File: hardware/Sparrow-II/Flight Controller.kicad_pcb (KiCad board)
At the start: 4 copper layers, 42 x 42 mm, 114 parts

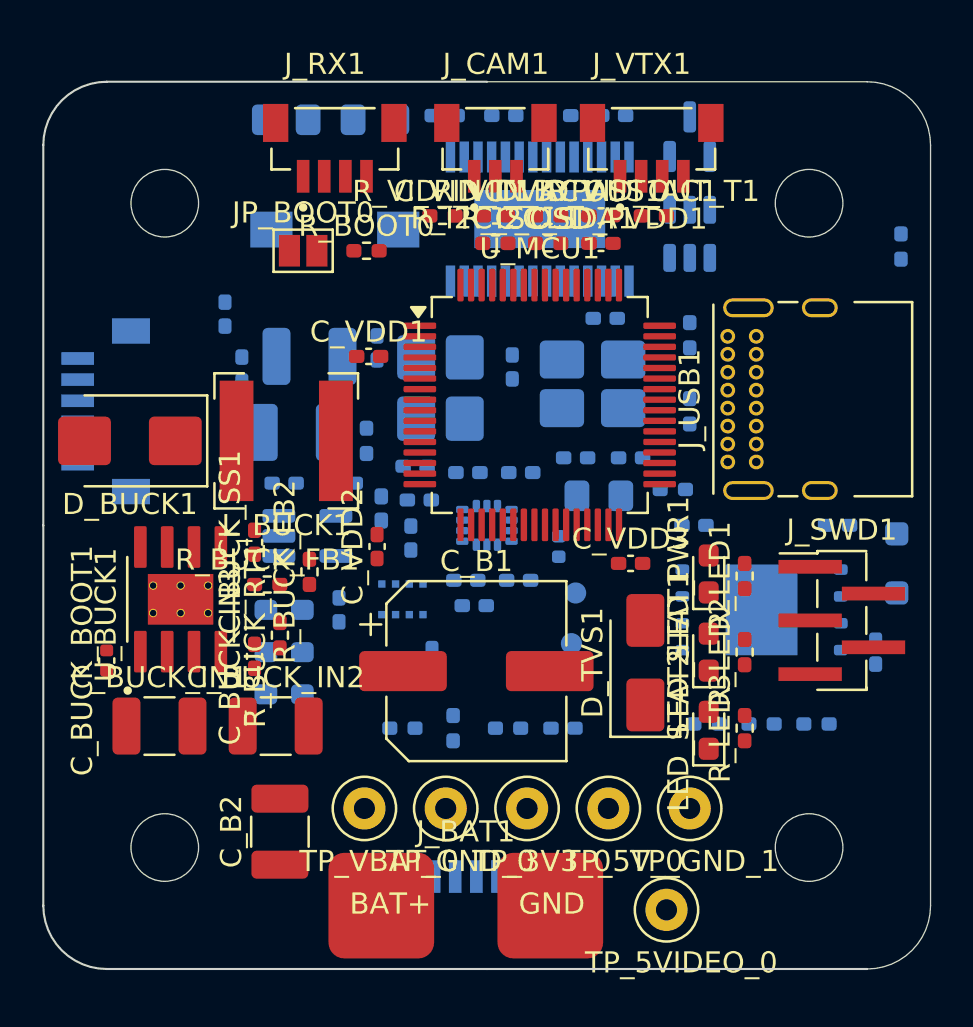
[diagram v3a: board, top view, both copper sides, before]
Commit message: hardware: BOM actualization and second layout
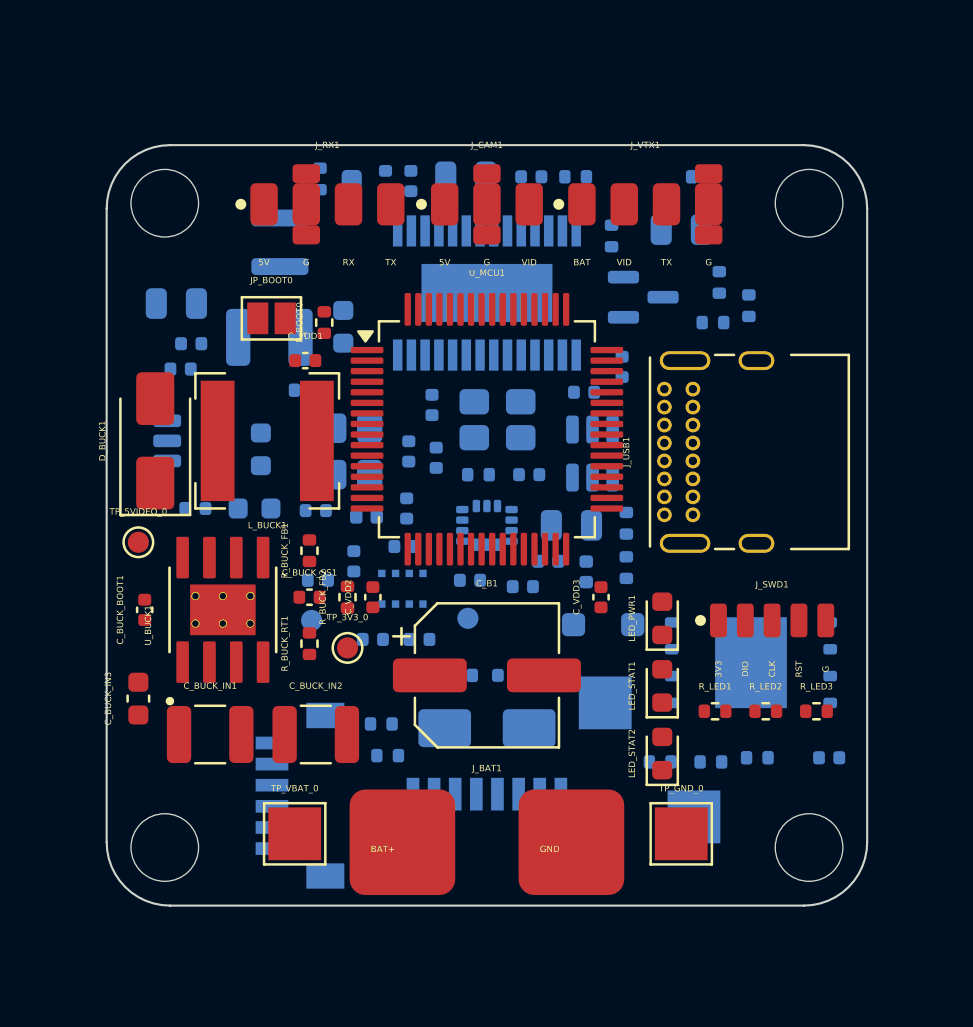
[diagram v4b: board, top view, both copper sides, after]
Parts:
- removed C_B2: 10uF, Capacitor_SMD:C_1210_3225Metric_Pad1.33x2.70mm_HandSolder
- removed C_B3: 1uF, Capacitor_SMD:C_0603_1608Metric_Pad1.08x0.95mm_HandSolder
- removed C_B4: 100nF, Capacitor_SMD:C_0402_1005Metric_Pad0.74x0.62mm_HandSolder
- removed C_BUCK_OUT2: 47uF, Capacitor_SMD:C_1210_3225Metric_Pad1.33x2.70mm_HandSolder
- removed C_USB_SH1: 10nF, Capacitor_SMD:C_0402_1005Metric_Pad0.74x0.62mm_HandSolder
- removed C_VID2: 22uF, Capacitor_SMD:C_0805_2012Metric_Pad1.18x1.45mm_HandSolder
- C_3V3_BULK1, C_5V_BULK1: footprint Capacitor_SMD:C_0603_1608Metric_Pad1.08x0.95mm_HandSolder -> Capacitor_SMD:C_0603_1608Metric
- C_B1: value 470uF -> 100uF; footprint Capacitor_SMD:CP_Elec_8x6.9 -> Capacitor_SMD:CP_Elec_6.3x7.7
- C_BARO1, C_BARO2, C_BUCK_SS1, C_CURR_F1, C_FLASH1, C_HSE1, C_HSE2, C_IMU_VDD1, C_IMU_VDD2, C_IMU_VIO1, C_IMU_VIO2, C_LDO_IN1, C_LDO_OUT1, C_NRST1, C_OSD_AVDD1, C_OSD_DVDD1, C_OSD_PVDD2, C_OSD_XTAL1, C_OSD_XTAL2, C_VBAT_ADC1, C_VDD1, C_VDD2, C_VDD3, C_VDD4, C_VDDA1, C_VDDA_HF1, C_VID3: footprint Capacitor_SMD:C_0402_1005Metric_Pad0.74x0.62mm_HandSolder -> Capacitor_SMD:C_0402_1005Metric
- C_BUCK_IN1, C_BUCK_IN2: value 2.2uF -> 4.7uF; footprint Capacitor_SMD:C_1210_3225Metric_Pad1.33x2.70mm_HandSolder -> Capacitor_SMD:C_1210_3225Metric
- C_BUCK_IN3, C_VDD_BULK1: footprint Capacitor_SMD:C_0402_1005Metric_Pad0.74x0.62mm_HandSolder -> Capacitor_SMD:C_0603_1608Metric
- C_BUCK_OUT1: footprint Capacitor_SMD:C_1210_3225Metric_Pad1.33x2.70mm_HandSolder -> Capacitor_SMD:C_1210_3225Metric
- C_OSD_PVDD1: footprint Capacitor_SMD:C_0402_1005Metric_Pad0.74x0.62mm_HandSolder -> Capacitor_SMD:C_0603_1608Metric; moved to B.Cu
- C_OSD_SAG1: footprint Capacitor_SMD:C_0402_1005Metric_Pad0.74x0.62mm_HandSolder -> Capacitor_SMD:C_0805_2012Metric
- C_VCAP1, C_VID1: footprint Capacitor_SMD:C_0805_2012Metric_Pad1.18x1.45mm_HandSolder -> Capacitor_SMD:C_0805_2012Metric
- C_VID_IN_AC1: footprint Capacitor_SMD:C_0402_1005Metric_Pad0.74x0.62mm_HandSolder -> Capacitor_SMD:C_0402_1005Metric; moved to B.Cu
- C_VID_OUT_AC1: footprint Capacitor_SMD:C_0402_1005Metric_Pad0.74x0.62mm_HandSolder -> Capacitor_SMD:C_0805_2012Metric; moved to B.Cu
- D_BUCK1: value B560C-13-F -> B260A-13-F; footprint Diode_SMD:D_SMB -> Diode_SMD:D_SMA
- D_TVS1: moved to B.Cu
- FB_VDDA1: footprint Inductor_SMD:L_0402_1005Metric_Pad0.77x0.64mm_HandSolder -> Inductor_SMD:L_0402_1005Metric
- J_CAM1: value BM03B-SRSS-TB_LF__SN_ -> CAM Pads; footprint SparrowHawk:JST_BM03B-SRSS-TB_LF__SN_ -> SparrowHawk:SolderPads_CAM_1x03
- J_RX1: value BM04B-SRSS-TB_LF__SN_ -> RX Pads; footprint SparrowHawk:JST_BM04B-SRSS-TB_LF__SN_ -> SparrowHawk:SolderPads_RX_1x04
- J_SWD1: value Conn_01x05 -> SWD Pads; footprint Connector_PinHeader_1.27mm:PinHeader_1x05_P1.27mm_Vertical_SMD_Pin1Left -> SparrowHawk:SolderPads_SWD_1x05
- J_VTX1: value BM04B-SRSS-TB_LF__SN_ -> VTX Pads; footprint SparrowHawk:JST_BM04B-SRSS-TB_LF__SN_ -> SparrowHawk:SolderPads_VTX_1x04
- LED_PWR1, LED_STAT1, LED_STAT2: footprint LED_SMD:LED_0603_1608Metric_Pad1.05x0.95mm_HandSolder -> LED_SMD:LED_0603_1608Metric
- L_VID1: footprint Inductor_SMD:L_Wuerth_WE-PD-Typ-7345 -> Inductor_SMD:L_Sunlord_SWPA3015S
- R_BOOT0, R_BUCK_FB1, R_BUCK_FB2, R_BUCK_RT1, R_CC1, R_CC2, R_CURR_F1, R_FLASH_CS1, R_FLASH_HD1, R_FLASH_WP1, R_HSE1, R_HSE2, R_LED1, R_LED2, R_LED3, R_OSD_RST1, R_VBAT_D1, R_VBAT_D2: footprint Resistor_SMD:R_0402_1005Metric_Pad0.72x0.64mm_HandSolder -> Resistor_SMD:R_0402_1005Metric
- R_I2C_SCL1, R_I2C_SDA1, R_VID_BYPASS1, R_VID_IN_T1, R_VID_OUT_T1: footprint Resistor_SMD:R_0402_1005Metric_Pad0.72x0.64mm_HandSolder -> Resistor_SMD:R_0402_1005Metric; moved to B.Cu
- R_USB_SH1: value 1M -> 0R; footprint Resistor_SMD:R_0402_1005Metric_Pad0.72x0.64mm_HandSolder -> Resistor_SMD:R_0402_1005Metric
- TP_3V3_0, TP_5VIDEO_0: value Test Point Loop -> Test Point; footprint TestPoint:TestPoint_Loop_D1.80mm_Drill1.0mm_Beaded -> TestPoint:TestPoint_Pad_D1.0mm
- TP_5V_0, TP_GND_1: value Test Point Loop -> Solder Pad; footprint TestPoint:TestPoint_Loop_D1.80mm_Drill1.0mm_Beaded -> TestPoint:TestPoint_Pad_2.5x2.5mm; moved to B.Cu
- TP_GND_0, TP_VBAT_0: value Test Point Loop -> Solder Pad; footprint TestPoint:TestPoint_Loop_D1.80mm_Drill1.0mm_Beaded -> TestPoint:TestPoint_Pad_2.5x2.5mm
- U_LDO1: footprint Package_TO_SOT_SMD:SOT-23-5_HandSoldering -> Package_TO_SOT_SMD:SOT-23-5
- Y_HSE1, Y_OSD1: footprint Crystal:Crystal_SMD_3225-4Pin_3.2x2.5mm_HandSoldering -> Crystal:Crystal_SMD_3225-4Pin_3.2x2.5mm
- moved TP_5VIDEO_0 30.5 mm to (133.5, 100.8)
- moved J_GPS1 20.4 mm to (141.6, 112.8)
- moved R_CC2 18.5 mm to (156.6, 99.9)
- moved D_USB_VBUS1 14.2 mm to (155.5, 104.7), turned to 0 degrees
- moved TP_VBAT_ADC_0 12.3 mm to (141.7, 104.5)
- moved C_OSD_PVDD1 12.0 mm to (143.6, 84.4), turned to 90 degrees
- moved C_5V_BULK1 11.7 mm to (139.3, 96.4), turned to 90 degrees
- moved TP_3V3_0 11.4 mm to (143.4, 105.8)
- moved U_ESD1 11.4 mm to (155.0, 96.6)
- moved TP_GND_0 11.2 mm to (159.2, 114.6)
- moved R_I2C_SCL1 11.0 mm to (160.7, 90.4)
- moved C_VBAT_ADC1 10.6 mm to (142.0, 102.6), turned to 0 degrees
- moved C_VID1 10.1 mm to (135.3, 89.5)
- moved R_I2C_SDA1 9.95 mm to (162.4, 89.6), turned to 90 degrees
- moved R_HSE1 9.23 mm to (149.6, 97.6)
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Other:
- board size 42 x 42 mm -> 36 x 36 mm

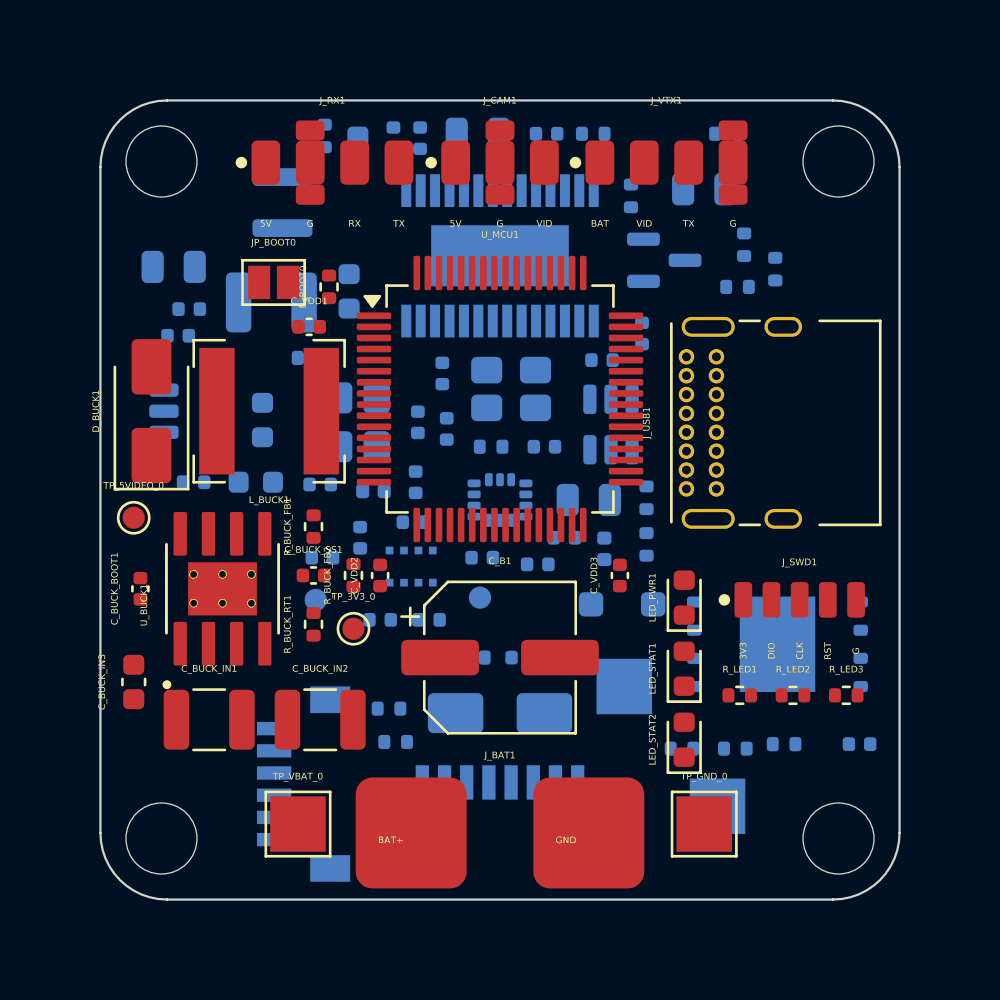
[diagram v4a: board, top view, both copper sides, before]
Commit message: hardware: Layout improvement
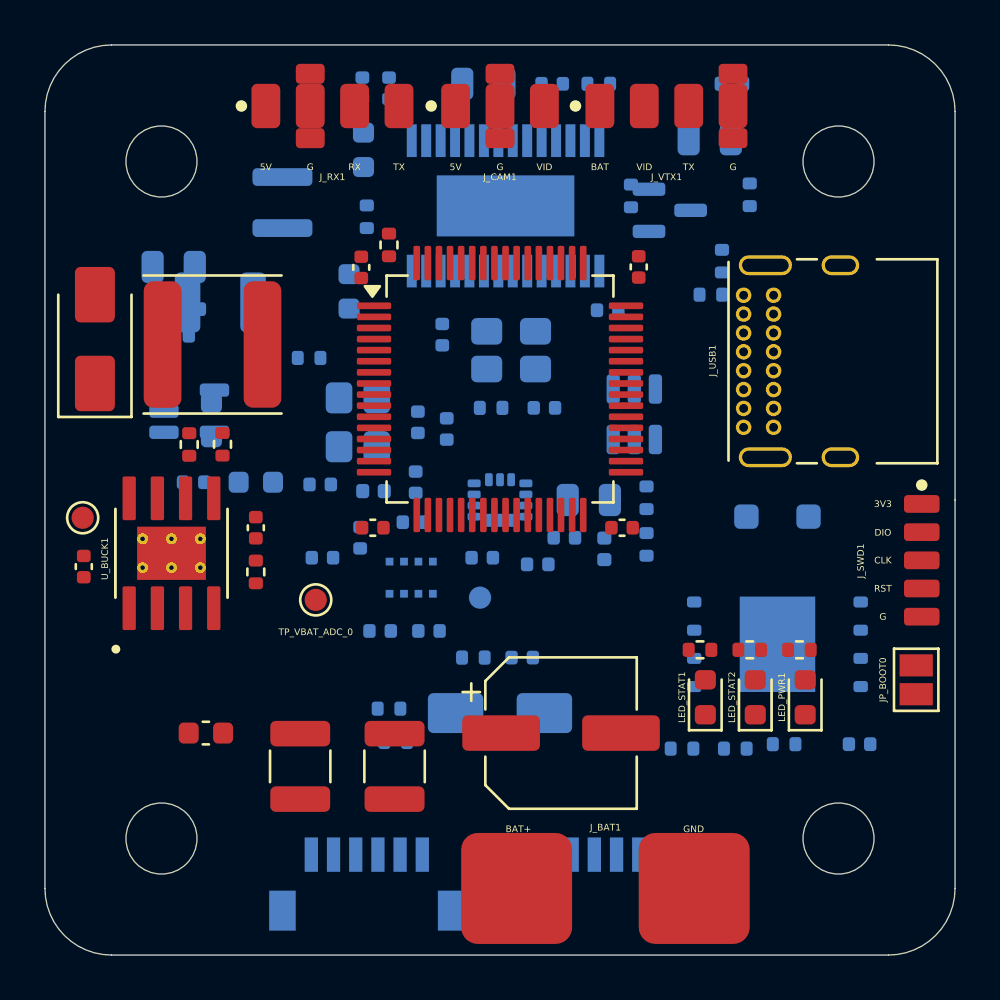
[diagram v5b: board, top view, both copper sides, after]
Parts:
- removed TP_3V3_0: Test Point, TestPoint:TestPoint_Pad_D1.0mm
- removed TP_5V_0, TP_GND_0, TP_GND_1, TP_VBAT_0: Solder Pad, TestPoint:TestPoint_Pad_2.5x2.5mm
- C_VDD4, TP_VBAT_ADC_0: moved to F.Cu
- L_BUCK1: footprint Inductor_SMD:L_Bourns-SRN6028 -> SparrowHawk:L_Sunlord_SWPA6028S
- moved JP_BOOT0 34.0 mm to (168.8, 108.1), turned to 90 degrees
- moved R_BUCK_FB2 8.35 mm to (137.5, 97.5), turned to -90 degrees
- moved D_USB_VBUS1 8.04 mm to (162.5, 100.8)
- moved LED_PWR1 7.06 mm to (163.8, 108.9)
- moved R_BUCK_FB1 6.71 mm to (136.0, 97.5)
- moved J_ESC1 6.60 mm to (155.8, 117.8)
- moved J_SWD1 5.78 mm to (169.0, 102.7), turned to -90 degrees
- moved J_GPS1 5.50 mm to (144.0, 117.8), turned to 0 degrees
- moved J_BAT1 5.37 mm to (154.8, 117.5)
- moved R_LED3 4.81 mm to (161.2, 106.8)
- moved R_LED2 4.66 mm to (159.0, 106.8)
- moved C_BUCK_IN1 4.61 mm to (141.0, 112.0), turned to -90 degrees
- moved C_B1 4.37 mm to (152.8, 110.5)
- moved D_BUCK1 4.13 mm to (131.8, 92.8)
- moved R_OSD_RST1 4.11 mm to (144.0, 87.2), turned to -90 degrees
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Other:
- board size 36 x 36 mm -> 41 x 41 mm

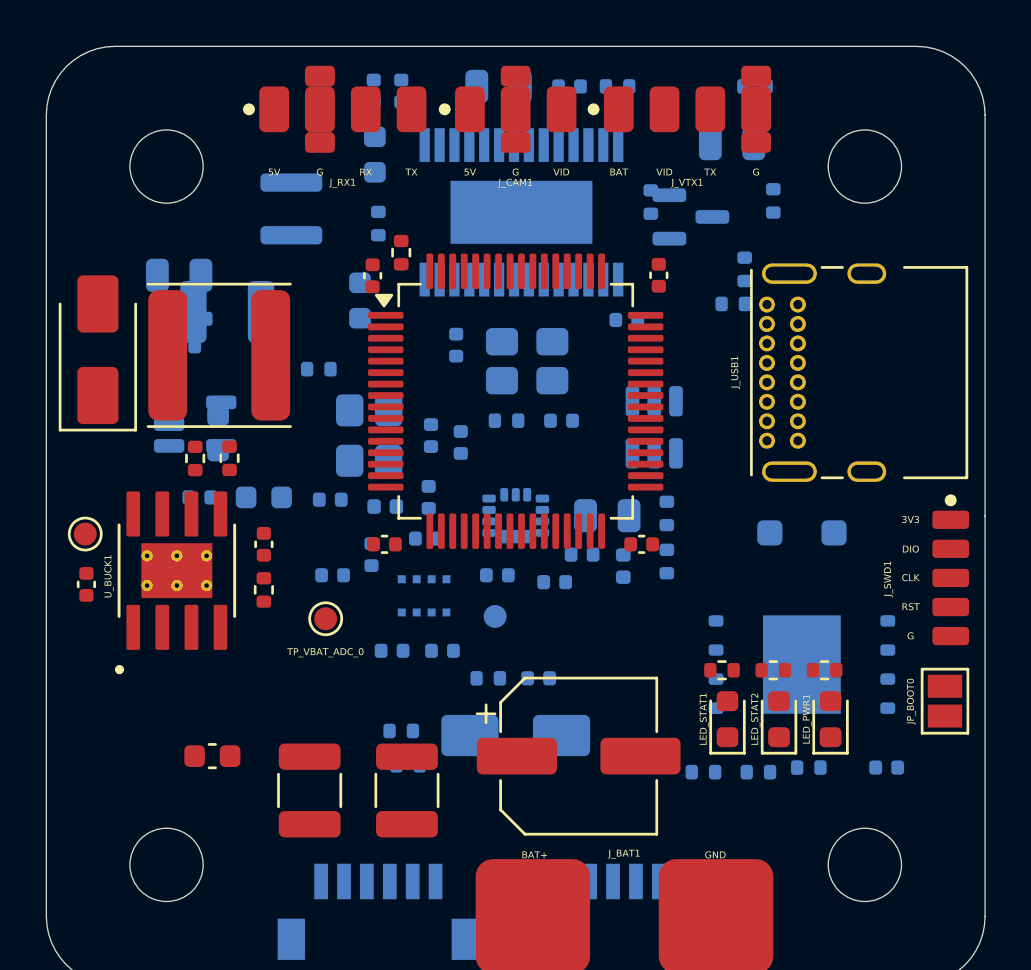
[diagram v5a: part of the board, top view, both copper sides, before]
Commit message: hardware: Fixes in layout
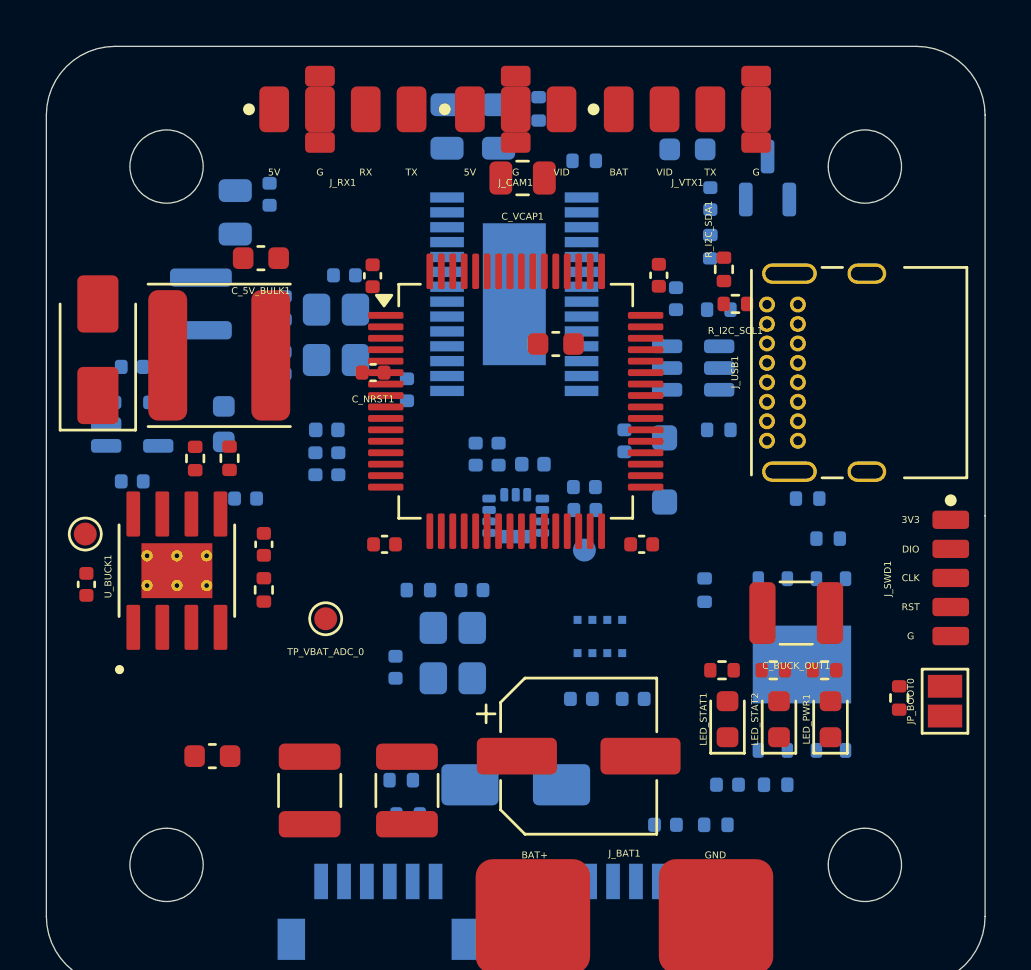
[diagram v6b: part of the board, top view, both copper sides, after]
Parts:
- C_5V_BULK1, C_BUCK_OUT1, C_NRST1, C_VCAP1, C_VDD_BULK1, R_I2C_SCL1, R_I2C_SDA1: moved to F.Cu
- moved R_BOOT0 29.2 mm to (166.8, 108.0)
- moved C_BUCK_OUT1 28.1 mm to (162.2, 104.2), turned to 180 degrees
- moved C_OSD_PVDD2 18.8 mm to (154.8, 96.7), turned to -90 degrees
- moved C_VCAP1 15.2 mm to (150.3, 85.2), turned to 180 degrees
- moved C_OSD_AVDD1 15.0 mm to (157.0, 90.5)
- moved C_OSD_PVDD1 13.7 mm to (157.5, 84.0), turned to 0 degrees
- moved C_VID_OUT_AC1 12.5 mm to (147.0, 83.0), turned to 90 degrees
- moved C_OSD_XTAL2 12.4 mm to (139.9, 93.3), turned to -90 degrees
- moved R_CURR_F1 11.8 mm to (158.7, 113.5)
- moved R_HSE1 10.9 mm to (139.9, 90.9), turned to -90 degrees
- moved R_FLASH_WP1 10.6 mm to (163.6, 101.0), turned to 180 degrees
- moved R_HSE2 10.6 mm to (145.8, 103.2)
- moved R_CC1 10.4 mm to (158.9, 96.2), turned to 180 degrees
- moved C_HSE2 10.2 mm to (144.8, 106.6), turned to -90 degrees
- moved Y_HSE1 10.2 mm to (147.2, 106.0), turned to -90 degrees
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
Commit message: hardware: Capacitors change
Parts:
- R_I2C_SCL1, R_I2C_SDA1: moved to B.Cu
- moved C_VCAP1 20.7 mm to (154.5, 105.5)
- moved R_I2C_SCL1 16.6 mm to (143.5, 86.8), turned to 0 degrees
- moved R_I2C_SDA1 15.6 mm to (143.5, 88.0), turned to 180 degrees
- moved C_VDD_BULK1 13.3 mm to (151.0, 105.8)
- moved C_NRST1 4.35 mm to (142.8, 89.5), turned to 90 degrees

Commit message: hardware: layout checkpoint 1
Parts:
- C_BUCK_SS1, JP_BOOT0, R_BOOT0, R_BUCK_FB1, R_BUCK_FB2, R_BUCK_RT1: moved to B.Cu
- D_USB_VBUS1, R_FLASH_CS1, R_USB_SH1: moved to F.Cu
- moved R_BOOT0 33.7 mm to (142.2, 84.8)
- moved JP_BOOT0 33.2 mm to (144.3, 85.6)
- moved R_CURR_F1 23.3 mm to (141.2, 98.2), turned to 90 degrees
- moved R_I2C_SCL1 22.4 mm to (152.1, 107.5)
- moved C_BUCK_OUT1 22.1 mm to (140.6, 100.3), turned to 0 degrees
- moved C_CURR_F1 20.1 mm to (142.8, 98.8), turned to 0 degrees
- moved J_ESC1 17.1 mm to (167.3, 105.2), turned to 90 degrees
- moved R_I2C_SDA1 16.9 mm to (150.5, 103.3), turned to 0 degrees
- moved C_HSE1 12.9 mm to (139.8, 93.3), turned to 90 degrees
- moved R_VBAT_D2 12.9 mm to (145.1, 100.2)
- moved Y_HSE1 12.3 mm to (142.3, 94.7), turned to 90 degrees
- moved C_HSE2 12.2 mm to (139.8, 95.5), turned to 90 degrees
- moved R_VBAT_D1 11.8 mm to (142.8, 100.0)
- moved C_VBAT_ADC1 8.55 mm to (146.8, 99.4), turned to 90 degrees
- moved C_BUCK_IN1 8.02 mm to (133.6, 108.9)
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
